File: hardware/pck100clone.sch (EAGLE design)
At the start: 222 parts, among them IC1 LM358N, IC3 LM358N, IC4 LM358N, IC5 LM358N, Q1 2SC945, Q2 2SC945, Q3 2N3906, Q4 2N3906, Q5 2N3904, Q6 2N3904

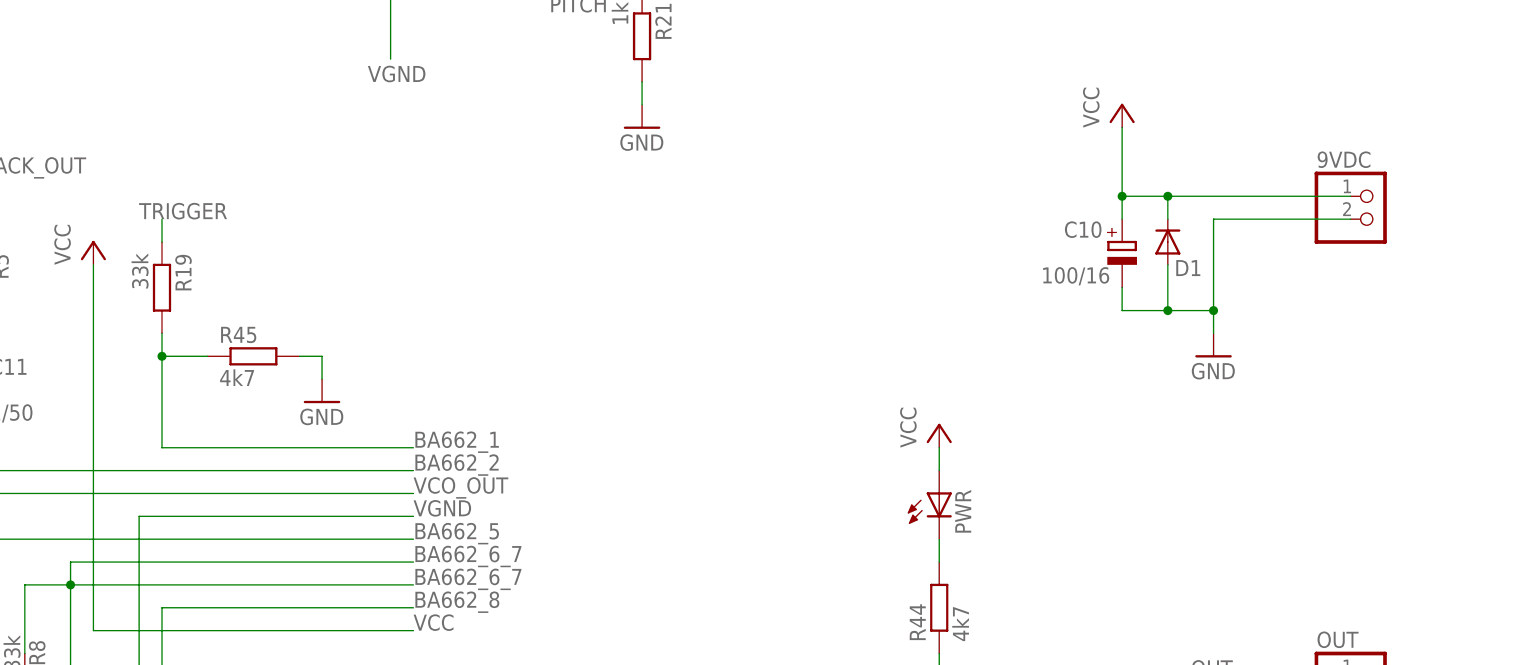
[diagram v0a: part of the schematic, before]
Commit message: REV4
add vca input trim / add series polarity diode
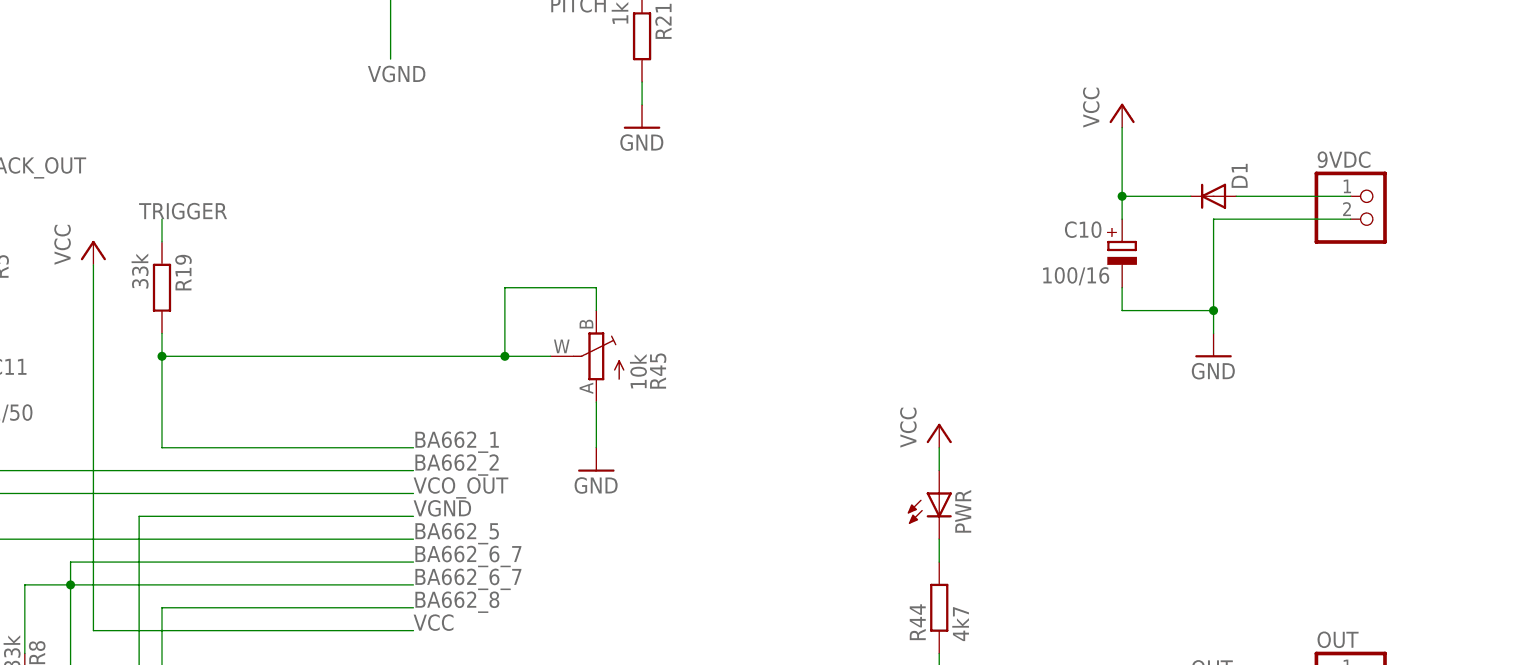
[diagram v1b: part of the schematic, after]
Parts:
- R45: value 4k7 -> 10k; device rcl:R-EU_0207/7 -> jason_eagle6:TRIM_EU-
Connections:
- new net N$2: 9VDC.1, D1.A
- net BA662_1: now also R45.E, R45.S; no longer R45.1
- net GND: now also R45.A; no longer D1.A, R45.2
- net VCC: no longer 9VDC.1
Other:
- moved on the sheet: D1
